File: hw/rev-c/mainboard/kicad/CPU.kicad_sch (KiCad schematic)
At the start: 12 parts, among them SW1 RESET, SW2 NMI, U1 W65C02S, U2 AS6C1008

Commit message: hw: fix wire/grid violations in schematic
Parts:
- U1: symbol Mainboard-rescue:W65C02SxP-PET -> EconoPET:W65C02S
- U2: symbol Mainboard-rescue:AS6C1008-PET -> EconoPET:AS6C1008
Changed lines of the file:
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@@
 	)
 	(symbol
-		(lib_id "Mainboard-rescue:W65C02SxP-PET")
+		(lib_id "EconoPET:W65C02S")
 		(at 92.71 106.68 0)
 		(unit 1)
@@
 	)
 	(symbol
-		(lib_id "Mainboard-rescue:AS6C1008-PET")
+		(lib_id "EconoPET:AS6C1008")
 		(at 187.96 97.79 0)
 		(unit 1)

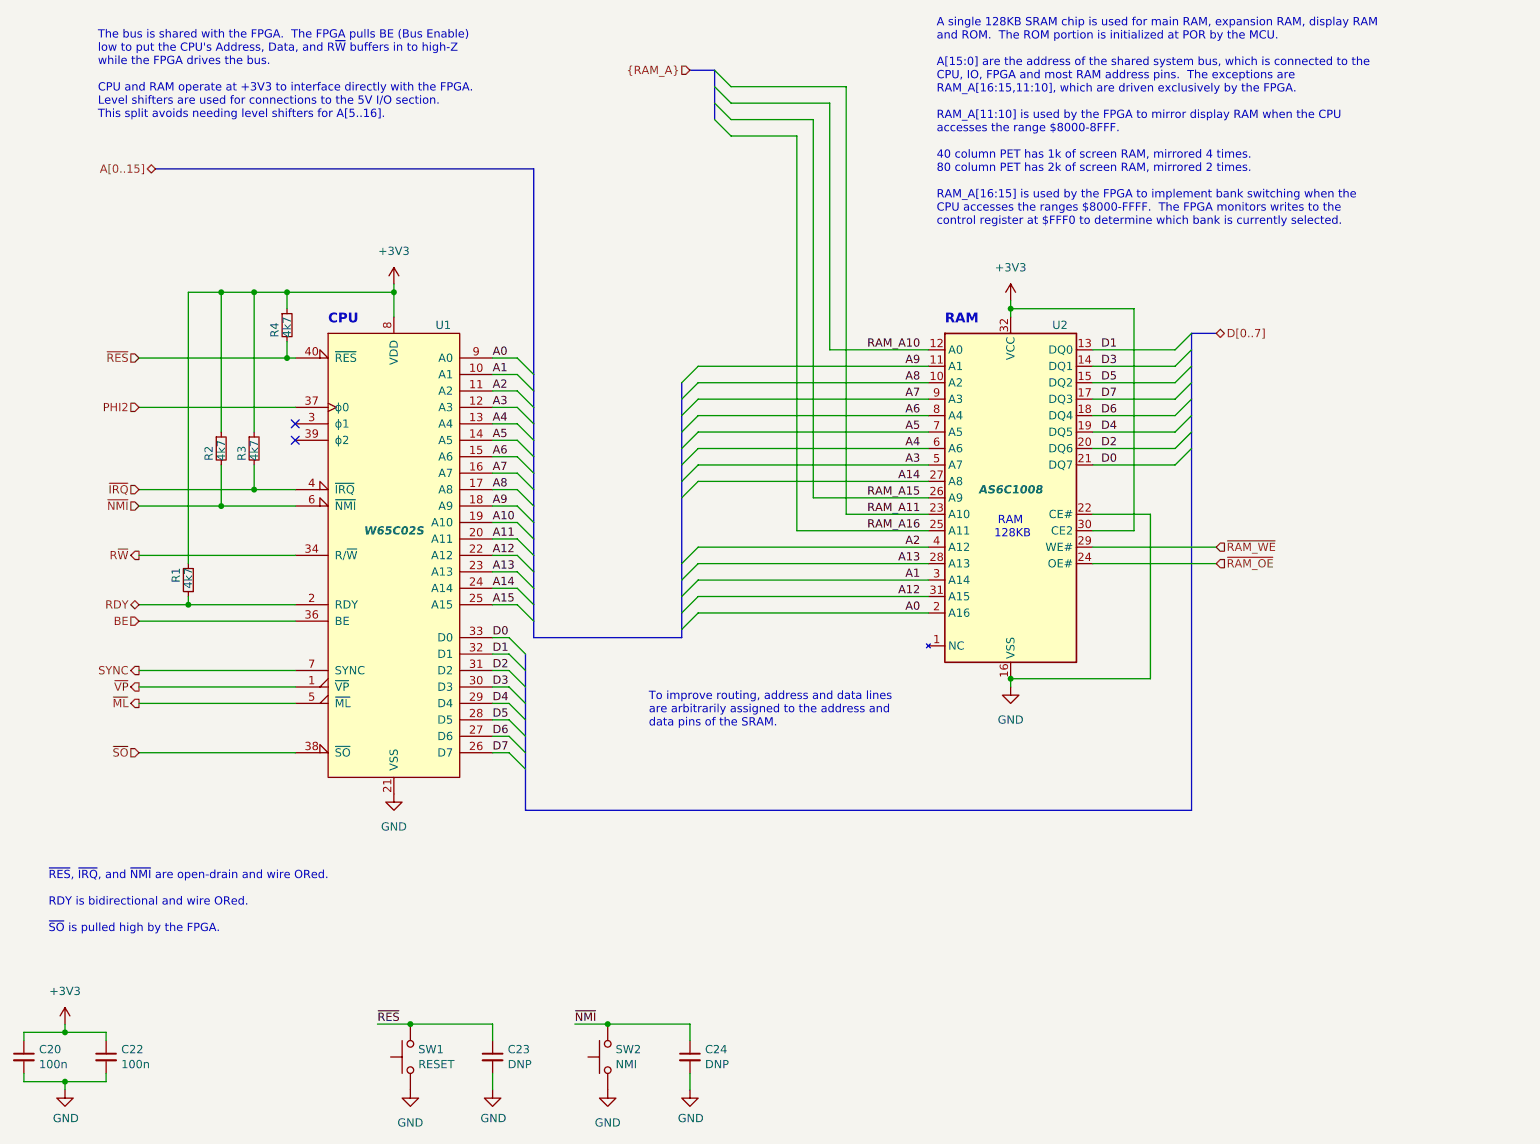
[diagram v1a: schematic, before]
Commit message: hw: renumber reference designators
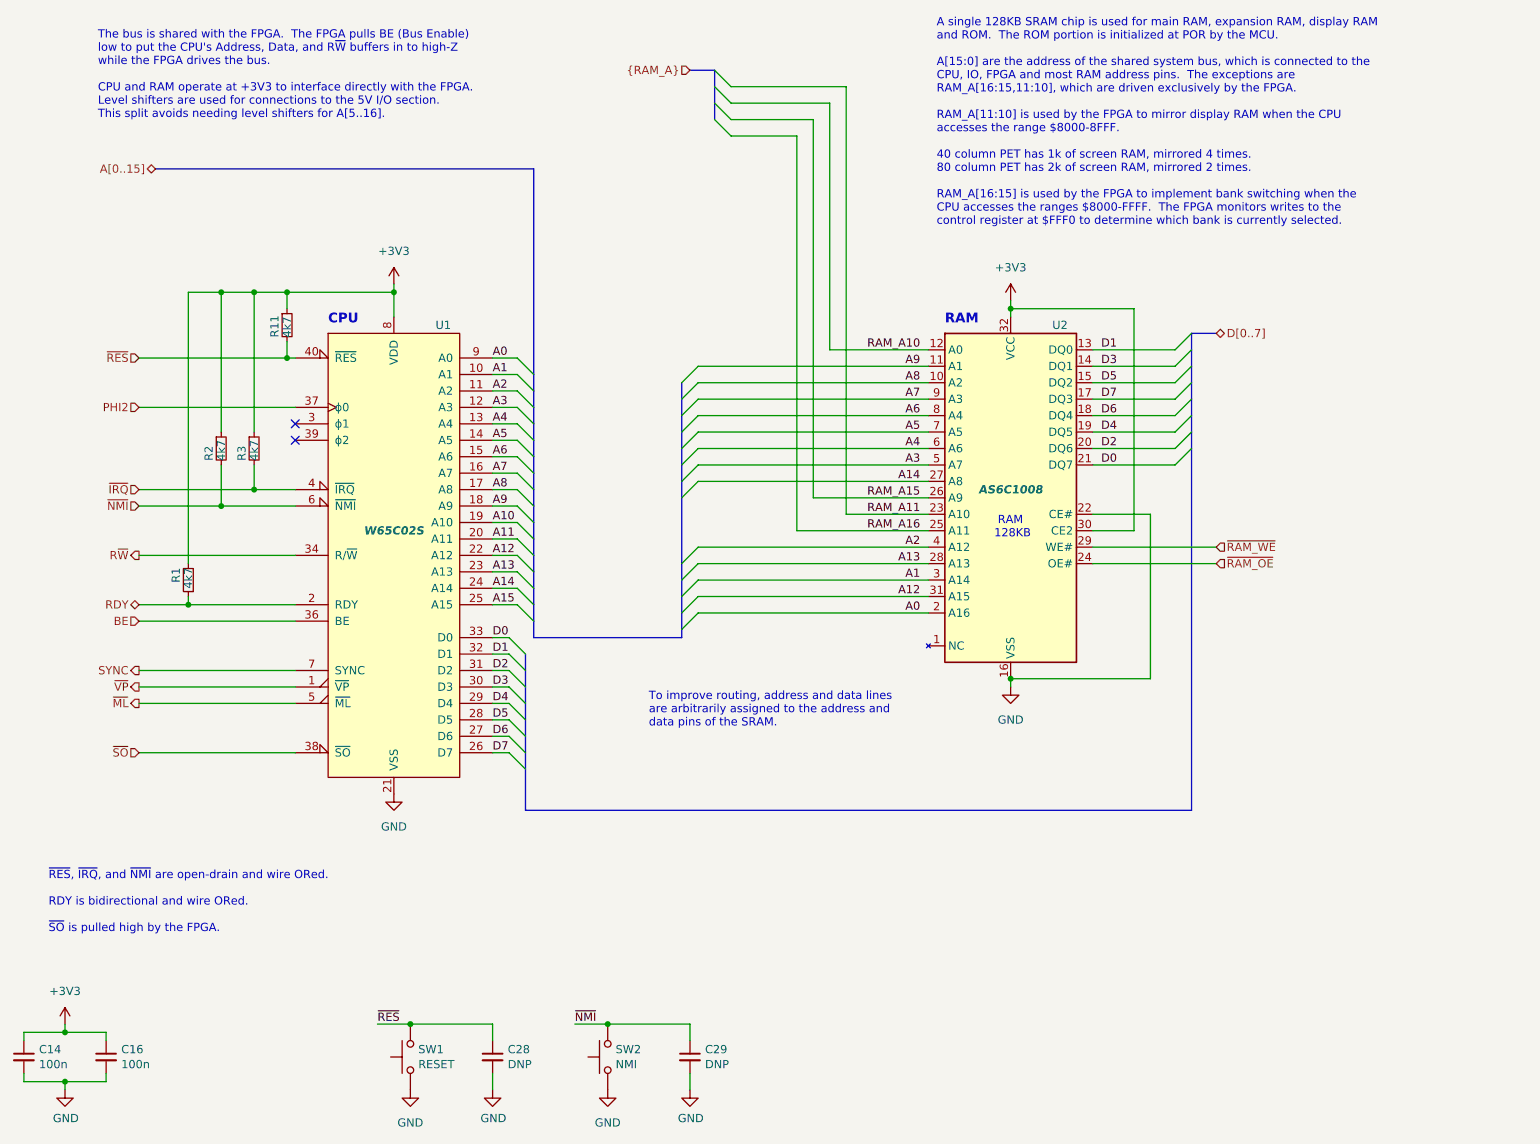
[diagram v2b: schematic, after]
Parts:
- renumbered C20 to C14, C22 to C16, C23 to C28, C24 to C29, R4 to R11
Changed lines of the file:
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@@
 		(on_board yes)
 		(dnp no)
-		(property "Reference" "C20"
+		(property "Reference" "C14"
 			(at 37.8968 182.9816 0)
 			(effects
@@
 			(project ""
 				(path "/2eea20e6-112c-411a-b615-885ae773135a/00000000-0000-0000-0000-0000614e685e"
-					(reference "C20")
+					(reference "C14")
 					(unit 1)
 				)
@@
 		(on_board yes)
 		(dnp no)
-		(property "Reference" "C22"
+		(property "Reference" "C16"
 			(at 50.5968 182.9816 0)
 			(effects
@@
 			(project ""
 				(path "/2eea20e6-112c-411a-b615-885ae773135a/00000000-0000-0000-0000-0000614e685e"
-					(reference "C22")
+					(reference "C16")
 					(unit 1)
 				)
@@
 		(on_board yes)
 		(dnp no)
-		(property "Reference" "R4"
+		(property "Reference" "R11"
 			(at 74.295 73.025 90)
 			(effects
@@
 			(project ""
 				(path "/2eea20e6-112c-411a-b615-885ae773135a/00000000-0000-0000-0000-0000614e685e"
-					(reference "R4")
+					(reference "R11")
 					(unit 1)
 				)
@@
 		(on_board yes)
 		(dnp no)
-		(property "Reference" "C23"
+		(property "Reference" "C28"
 			(at 110.2868 182.9816 0)
 			(effects
@@
 			(project ""
 				(path "/2eea20e6-112c-411a-b615-885ae773135a/00000000-0000-0000-0000-0000614e685e"
-					(reference "C23")
+					(reference "C28")
 					(unit 1)
 				)
@@
 		(on_board yes)
 		(dnp no)
-		(property "Reference" "C24"
+		(property "Reference" "C29"
 			(at 140.7668 182.9816 0)
 			(effects
@@
 			(project ""
 				(path "/2eea20e6-112c-411a-b615-885ae773135a/00000000-0000-0000-0000-0000614e685e"
-					(reference "C24")
-					(unit 1)
-				)
+					(reference "C29")
+					(unit 1)
+				)

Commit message: hw: match original PET designators for connectors
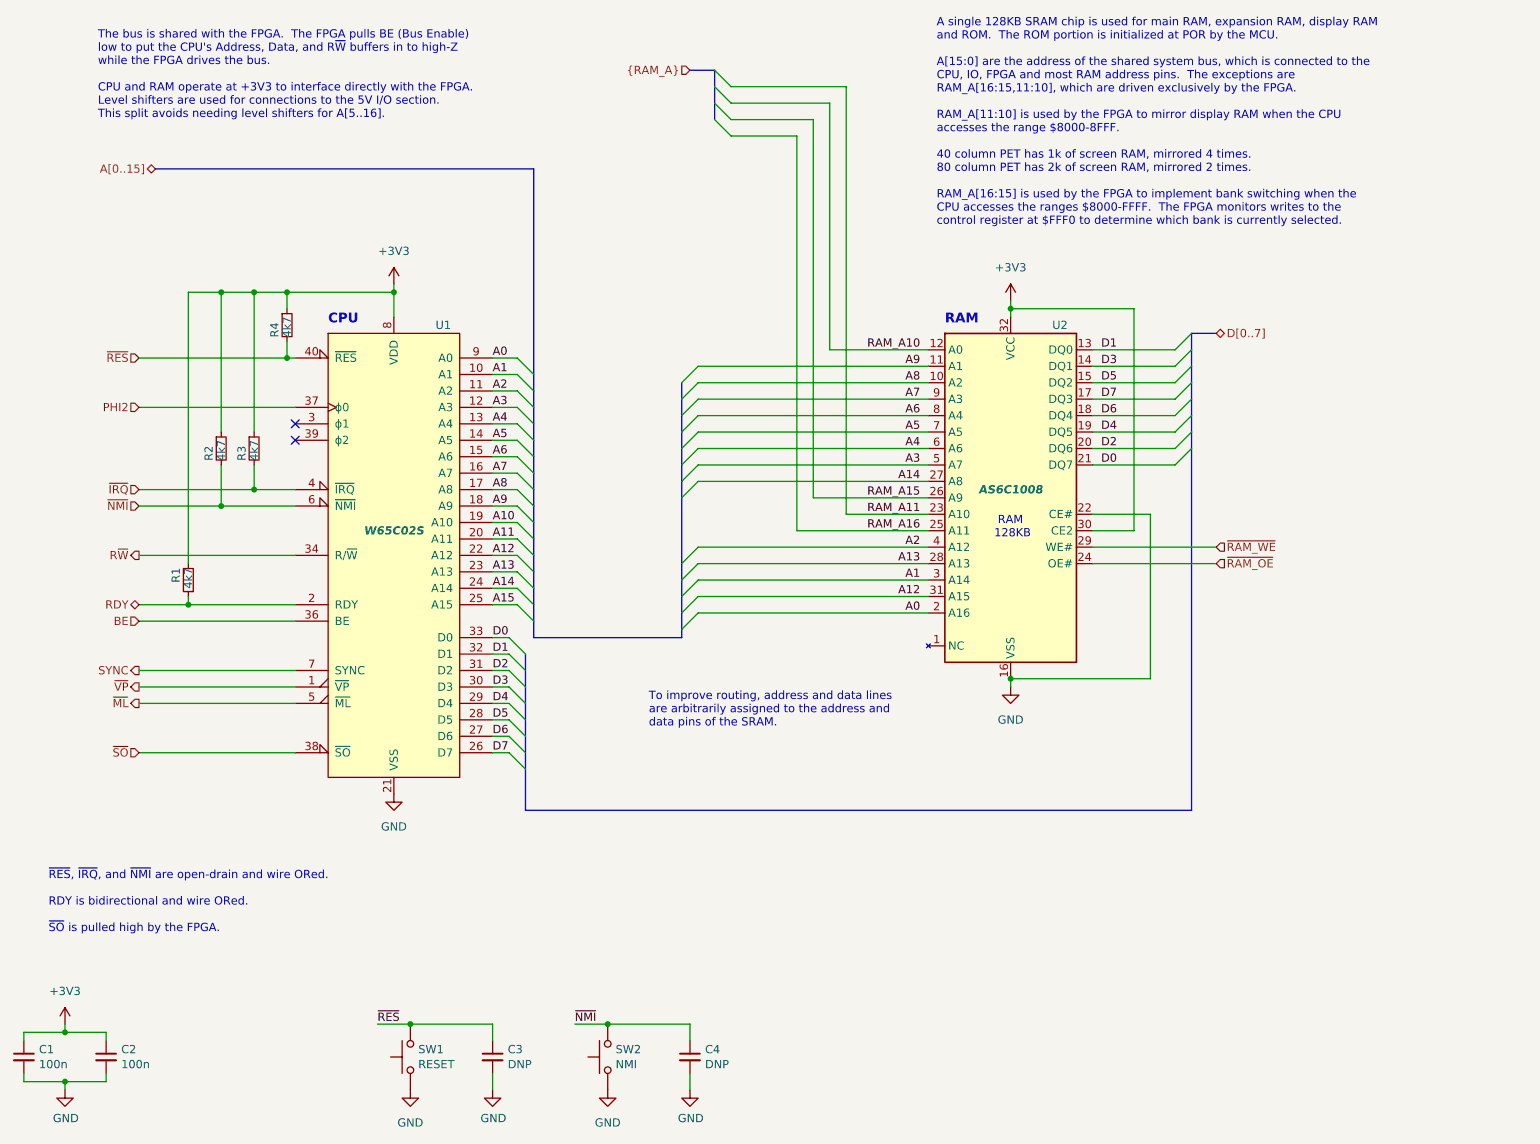
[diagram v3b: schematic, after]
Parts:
- renumbered C14 to C1, C16 to C2, C28 to C3, C29 to C4, R11 to R4
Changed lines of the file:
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@@
 		(on_board yes)
 		(dnp no)
-		(property "Reference" "C14"
+		(property "Reference" "C1"
 			(at 37.8968 182.9816 0)
 			(effects
@@
 			(project ""
 				(path "/2eea20e6-112c-411a-b615-885ae773135a/00000000-0000-0000-0000-0000614e685e"
-					(reference "C14")
+					(reference "C1")
 					(unit 1)
 				)
@@
 		(on_board yes)
 		(dnp no)
-		(property "Reference" "C16"
+		(property "Reference" "C2"
 			(at 50.5968 182.9816 0)
 			(effects
@@
 			(project ""
 				(path "/2eea20e6-112c-411a-b615-885ae773135a/00000000-0000-0000-0000-0000614e685e"
-					(reference "C16")
+					(reference "C2")
 					(unit 1)
 				)
@@
 		(on_board yes)
 		(dnp no)
-		(property "Reference" "R11"
+		(property "Reference" "R4"
 			(at 74.295 73.025 90)
 			(effects
@@
 			(project ""
 				(path "/2eea20e6-112c-411a-b615-885ae773135a/00000000-0000-0000-0000-0000614e685e"
-					(reference "R11")
+					(reference "R4")
 					(unit 1)
 				)
@@
 		(on_board yes)
 		(dnp no)
-		(property "Reference" "C28"
+		(property "Reference" "C3"
 			(at 110.2868 182.9816 0)
 			(effects
@@
 			(project ""
 				(path "/2eea20e6-112c-411a-b615-885ae773135a/00000000-0000-0000-0000-0000614e685e"
-					(reference "C28")
+					(reference "C3")
 					(unit 1)
 				)
@@
 		(on_board yes)
 		(dnp no)
-		(property "Reference" "C29"
+		(property "Reference" "C4"
 			(at 140.7668 182.9816 0)
 			(effects
@@
 			(project ""
 				(path "/2eea20e6-112c-411a-b615-885ae773135a/00000000-0000-0000-0000-0000614e685e"
-					(reference "C29")
-					(unit 1)
-				)
+					(reference "C4")
+					(unit 1)
+				)

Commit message: hw: tidy warnings
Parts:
- C4: footprint Capacitor_SMD:C_0603_1608Metric -> Capacitor_SMD:C_0402_1005Metric; LCSC C96446 -> (none)
- C89: renamed from C3; footprint Capacitor_SMD:C_0603_1608Metric -> Capacitor_SMD:C_0402_1005Metric; LCSC C96446 -> (none)
- SW1, SW2: footprint JLCPCB:SW-TH_L6.0-W3.5-P6.50 -> EconoPET:SW_PUSH_1P1T_6x3.5mm_H4.3_APEM_MJTP1243
- renumbered C1 to C100, C2 to C104
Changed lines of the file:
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@@
 		(on_board yes)
 		(dnp no)
-		(property "Reference" "C1"
+		(property "Reference" "C100"
 			(at 37.8968 182.9816 0)
 			(effects
@@
 			(project ""
 				(path "/2eea20e6-112c-411a-b615-885ae773135a/00000000-0000-0000-0000-0000614e685e"
-					(reference "C1")
+					(reference "C100")
 					(unit 1)
 				)
@@
 		(on_board yes)
 		(dnp no)
-		(property "Reference" "C2"
+		(property "Reference" "C104"
 			(at 50.5968 182.9816 0)
 			(effects
@@
 			(project ""
 				(path "/2eea20e6-112c-411a-b615-885ae773135a/00000000-0000-0000-0000-0000614e685e"
-					(reference "C2")
+					(reference "C104")
 					(unit 1)
 				)
@@
 		(on_board yes)
 		(dnp no)
-		(property "Reference" "C3"
+		(property "Reference" "C89"
 			(at 110.2868 182.9816 0)
 			(effects
@@
 			)
 		)
-		(property "Footprint" "Capacitor_SMD:C_0603_1608Metric"
+		(property "Footprint" "Capacitor_SMD:C_0402_1005Metric"
 			(at 107.95 184.15 0)
 			(effects
@@
 			)
 		)
-		(property "Datasheet" "https://datasheet.lcsc.com/lcsc/2304140030_Samsung-Electro-Mechanics-CL10A106MA8NRNC_C96446.pdf"
+		(property "Datasheet" ""
 			(at 107.95 184.15 0)
 			(effects
@@
 			)
 		)
-		(property "LCSC" "C96446"
+		(property "LCSC" ""
 			(at 107.95 184.15 0)
 			(effects
@@
 			(project ""
 				(path "/2eea20e6-112c-411a-b615-885ae773135a/00000000-0000-0000-0000-0000614e685e"
-					(reference "C3")
+					(reference "C89")
 					(unit 1)
 				)
@@
 			)
 		)
-		(property "Footprint" "JLCPCB:SW-TH_L6.0-W3.5-P6.50"
+		(property "Footprint" "EconoPET:SW_PUSH_1P1T_6x3.5mm_H4.3_APEM_MJTP1243"
 			(at 90.17 184.15 0)
 			(effects
@@
 			)
 		)
-		(property "Footprint" "JLCPCB:SW-TH_L6.0-W3.5-P6.50"
+		(property "Footprint" "EconoPET:SW_PUSH_1P1T_6x3.5mm_H4.3_APEM_MJTP1243"
 			(at 120.65 184.15 0)
 			(effects
@@
 			)
 		)
-		(property "Footprint" "Capacitor_SMD:C_0603_1608Metric"
+		(property "Footprint" "Capacitor_SMD:C_0402_1005Metric"
 			(at 138.43 184.15 0)
 			(effects
@@
 			)
 		)
-		(property "Datasheet" "https://datasheet.lcsc.com/lcsc/2304140030_Samsung-Electro-Mechanics-CL10A106MA8NRNC_C96446.pdf"
+		(property "Datasheet" ""
 			(at 138.43 184.15 0)
 			(effects
@@
 			)
 		)
-		(property "LCSC" "C96446"
+		(property "LCSC" ""
 			(at 138.43 184.15 0)
 			(effects

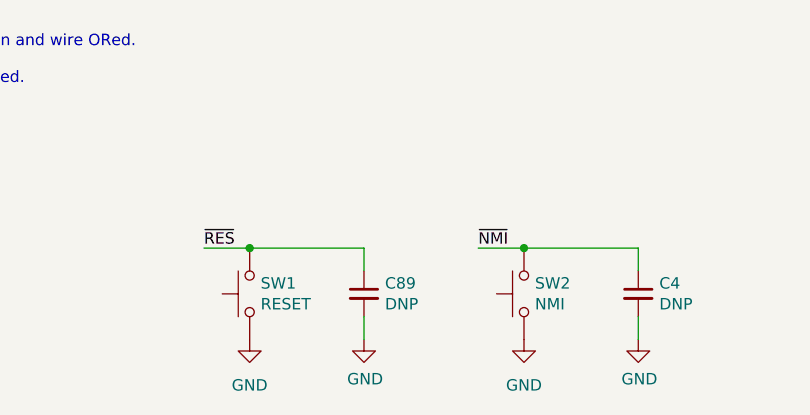
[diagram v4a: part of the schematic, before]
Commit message: hw: touchups and part names on back silk
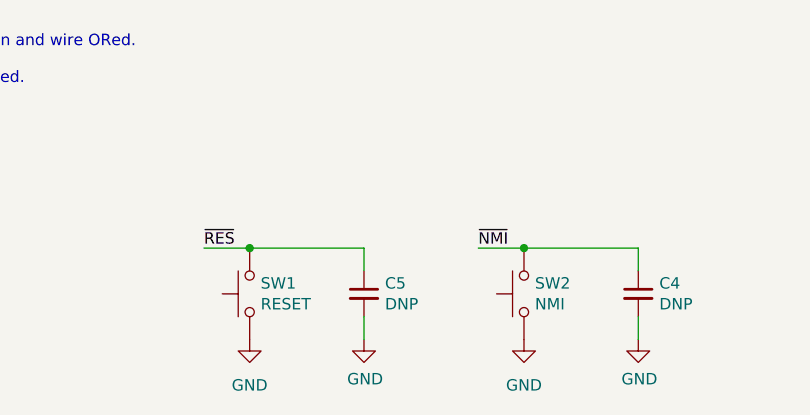
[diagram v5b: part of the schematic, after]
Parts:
- renumbered C89 to C5
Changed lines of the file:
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@@
 		(on_board yes)
 		(dnp no)
-		(property "Reference" "C89"
+		(property "Reference" "C5"
 			(at 110.2868 182.9816 0)
 			(effects
@@
 			(project ""
 				(path "/2eea20e6-112c-411a-b615-885ae773135a/00000000-0000-0000-0000-0000614e685e"
-					(reference "C89")
+					(reference "C5")
 					(unit 1)
 				)
